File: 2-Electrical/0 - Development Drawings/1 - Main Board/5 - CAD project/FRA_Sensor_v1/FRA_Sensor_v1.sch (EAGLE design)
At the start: 237 parts, among them IC1 CP2101, IC2 LMV611, IC3 TS520533, IC4 ADS1115BQDGSRQ1, IC5 ADS1115BQDGSRQ1, IC7 LMP91000SD_NOPB, IC8 PCA9555PW, IC9 LDK320ADU50R, J2 ETH_CONN, J5 WM9734TR-ND, J8 1140084168, Q1 Si2300DS, Q10 FDN306P, Q11 FDN306P, Q12 FDN306P, Q13 FDN306P, Q14 FDN306P, Q15 FDN306P, Q16 FDN306P, Q17 FDN306P, Q2 FDN306P, Q3 Si2300DS, Q5 FDN306P, Q6 FDN306P, Q7 100A/100V/6.8mΩ, Q8 FDN306P, Q9 FDN306P, T1 BC847, T2 BC847, T3 BC847, U1 PCA9509DP, U2 ESP-WROOM-32, X1 TB001-500-02BE, Y3 32.768kHz

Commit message: sch update layout update
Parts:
- removed C20, C22: 10u, resistor:C-EUC0603K
- removed C32, C33, C34: 100n, resistor:C-EUC0603K
- removed C35, C36: 1u, resistor:C-EUC0603K
- removed D3: BAS17, nxp_60:BAS17
- removed IC3: TS520533, v-reg:TS520533
- removed IC7: LMP91000SD_NOPB, SamacSys_Parts:LMP91000SD_NOPB
- removed Q1: Si2300DS, adafruit:MOSFET-NREFLOW
- removed Q16, Q17: FDN306P, microbuilder:MOSFET-PWIDE
- removed R33, R66, R79, R80: 10k, resistor:R-EU_R0603
- removed R34, R35, R36: 47k, resistor:R-EU_R0603
- removed R37: 27k, resistor:R-EU_R0603
- removed R38: 0, resistor:R-EU_R0603
- removed R39: 12k, resistor:R-EU_R0603
- removed R56: 5.1k, resistor:R-EU_R0603
- removed R57: 0R, resistor:R-EU_R0603
- removed R58, R60, R61, R62: (DNI), resistor:R-EU_R0603
- removed R59: 1M, resistor:R-EU_R0603
- removed S$1: CITIPEL_4P50, FRA_eagle_lib:CITIPEL_4P50
- removed S$2: FIGARO_2611, FRA_eagle_lib:FIGARO_2611
- removed T3: BC847, nxp_60:BC847
- removed T4: (no value), transistor-neu-to92:-NPN-SOT223
- removed TP18: TPTP10R, testpad:TPTP10R
- removed U$17, U$18: CONN_03X2_WE_61200621621, FRA_eagle_lib:CONN_03X2_WE_61200621621
- added R14: 0(DNI), resistor:R-EU_R0603
- added R15, R18: 10k, resistor:R-EU_R0603
- added SENSOR_D3: + G SCL SDA, pinhead:PINHD-1X4
- added TP21: TPTP10R, testpad:TPTP10R
- C18: value 1n -> 100n
- C19: value 10u -> 100n
- C37, C41: value 1u -> 10u
- C4: value 1u -> 100n
- IC2: value LMV611 -> ADS1115BQDGSRQ1; device linear:OPA333DCK -> SamacSys_Parts:ADS1115BQDGSRQ1
- R42: value 2k(NC) -> 10k
- R81, R82: value 10k -> 2k2
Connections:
- removed net 3V3_TGS2611: C36.1, IC3.VOUT, R61.2
- removed net AA1: R66.1
- removed net ADC3_3: U$17.2
- removed net ADC3_4: U$18.2
- removed net ADC_TGS2611: C33.1, R57.2, R58.2
- removed net ENB_PWR_IF11: Q16.G, R79.2
- removed net ENB_PWR_IF12: Q17.G, R80.2
- removed net EN_IF11: Q16.D, R79.1, U$17.4
- removed net EN_IF12: Q17.D, R80.1, U$18.4
- removed net N$12 (its old number): C22.1, C4.1, R66.2
- removed net N$13 (its old number): C22.2
- removed net N$14: C4.2
- removed net N$16: IC2.V+
- removed net N$17: R38.1
- removed net N$18: R34.2
- removed net N$26: R39.1, T3.B
- removed net N$27: C18.1
- removed net N$28: IC2.+IN, R34.1, R35.2
- removed net N$32: IC2.-IN, R36.2, R37.1
- removed net N$34: C19.1, R37.2
- removed net N$35: IC2.OUT, R36.1
- removed net N$36: C18.2, C19.2, R33.2, R39.2
- removed net N$46: IC8.I/O1.4, TP18.TP
- removed net N$53: Q1.D, S$2.1_RH
- removed net N$56: C34.1, IC3.CB
- removed net PWM: R33.1
- removed net RS_NEG: R56.1, R57.1, S$2.2_RS_N
- removed net RS_POS: C32.1, R60.2, R61.1, R62.1, S$2.3_RS_P
- removed net TGS2611_HEAT_EN: Q1.G, R59.1
- removed net VREF_TGS6211: R62.2
- new net 3AIN0: C18.1, IC2.AIN1, R15.1
- new net 3AIN1: C19.1, IC2.AIN2, R18.1
- new net N$7: IC2.ALERT/RDY, TP21.TP
- net +5V/1: now also C4.1, C42.1, IC2.VDD, R67.1, R70.1, R71.1, R72.1, R73.1, R74.1, R75.1, R76.1, R77.1, R78.1; no longer Q16.S, Q17.S
- net 1AIN0: now also IC5.AIN2; no longer IC5.AIN0
- net 1AIN1: now also IC5.AIN3; no longer IC5.AIN1
- net 1AIN2: now also IC5.AIN1; no longer IC5.AIN3
- net 1AIN3: now also IC5.AIN0; no longer IC5.AIN2
- net 2AIN0: now also IC4.AIN2; no longer IC4.AIN0
- net 2AIN1: now also IC4.AIN3; no longer IC4.AIN1
- net 2AIN2: now also IC4.AIN1; no longer IC4.AIN3
- net 2AIN3: now also IC4.AIN0; no longer IC4.AIN2
- net 5V: no longer C35.1, C42.1, IC3.CE, IC3.VIN, R60.1, S$2.4_RH
- net 5V_CALM: no longer U$17.3, U$18.3
- net ADC3_1: now also R15.2
- net ADC3_2: now also R18.2
- net AGND: now also C18.2, C19.2, C4.2, IC2.GND; no longer U$17.1, U$18.1
- net BTN1: now also R14.2
- net ENB_PWR_IF1: now also IC8.I/O0.6; no longer IC8.I/O0.0
- net ENB_PWR_IF10: now also IC8.I/O0.0
- net ENB_PWR_IF2: now also IC8.I/O0.7; no longer IC8.I/O0.1
- net ENB_PWR_IF7: now also IC8.I/O1.7; no longer IC8.I/O0.6
- net ENB_PWR_IF8: now also IC8.I/O1.6; no longer IC8.I/O0.7
- net ENB_PWR_IF9: now also IC8.I/O0.1
- net EN_IF1: no longer R67.1
- net EN_IF10: no longer R78.1
- net EN_IF2: no longer R70.1
- net EN_IF3: no longer R71.1
- net EN_IF4: no longer R72.1
- net EN_IF5: no longer R73.1
- net EN_IF6: no longer R74.1
- net EN_IF7: no longer R75.1
- net EN_IF8: no longer R76.1
- net EN_IF9: no longer R77.1
- net GND: no longer C32.2, C33.2, C34.2, C35.2, C36.2, IC3.GND, Q1.S, R38.2, R56.2, R58.1, R59.2, T3.E
- net NRST: now also R14.1
- net SCL_5V: now also IC2.ADDR, IC2.SCL; no longer U$17.6, U$18.6
- net SDA_5V: now also IC2.SDA; no longer U$17.5, U$18.5
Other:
- note added: "GY-21 Si7021 - T a RH addr:0x40"
- note added: "Molex 105133-0001"
- note added: "VEML7700 - Lux addr:0X10"
- note added: "pull-downs on sensor boards"
- note removed: "15.9kHz cutoff"
- note removed: "3.3V LDO"
- note removed: "Buzzer audio"
- note removed: "DNI"
- note removed: "For capacitance multiplier 621-FZT651QTC - 3A Ic 621-FZT851QTA - 6A Ic"
- note removed: "GY-21 Si7021 - T a RH addr:0x40 VEML7700 - Lux addr:0X10"
- note removed: "TODO LDO to 5V low noise supply"
- note removed: "alt. part LP5907"

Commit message: layout done,
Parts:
- renumbered SENSOR_D1 to S_D1, SENSOR_D2 to S_D2
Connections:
- removed net BTN2: U2.IO35
- new net N$14: IC2.AIN0, SENSOR_D3.3
- new net N$16: IC2.AIN3, SENSOR_D3.2
- net +5V/1: now also SENSOR_D3.4
- net AGND: now also SENSOR_D3.1
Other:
- moved on the sheet: SENSOR_D3

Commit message: updates
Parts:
- removed FID3: FIDUCIAL"", microbuilder:FIDUCIAL""
- added C20: 10u, resistor:C-EUC0603K
- added C22: 100n, resistor:C-EUC0603K
- added IC3: P82B715DR, SamacSys_Parts:P82B715DR
- added R33, R34: 330, resistor:R-EU_R0603
- R21: value 1M -> 100k
- R3: value 470 -> 100
- renumbered SENSOR_D3 to J9
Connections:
- new net SCL_BUFF: IC3.LY, R34.2, U$10.6, U$11.6, U$12.6, U$13.6, U$14.6, U$15.6, U$16.6, U$3.6, U$8.6, U$9.6
- new net SDA_BUFF: IC3.LX, R33.2, U$10.5, U$11.5, U$12.5, U$13.5, U$14.5, U$15.5, U$16.5, U$3.5, U$8.5, U$9.5
- net +5V/1: now also C20.1, C22.1, IC3.VCC, R33.1, R34.1
- net AGND: now also C20.2, C22.2, IC3.GND
- net SCL_5V: now also IC3.SY; no longer U$10.6, U$11.6, U$12.6, U$13.6, U$14.6, U$15.6, U$16.6, U$3.6, U$8.6, U$9.6
- net SDA_5V: now also IC3.SX; no longer U$10.5, U$11.5, U$12.5, U$13.5, U$14.5, U$15.5, U$16.5, U$3.5, U$8.5, U$9.5
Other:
- note added: "A3.0,A3.3"
- note added: "ADC1"
- note added: "ADC2"
- note added: "ADC3"
- note added: "I2C repeater"
- note added: "Pullup min 270R (due to sink current)"
- moved on the sheet: C18, C19, C21, C46, C47, C48, C49, C50, C51, C52, R15, R18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

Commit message: updates
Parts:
- removed J1: (no value), con-jack:JACK-PLUG1
- added J3: PJ-031C, SamacSys_Parts:PJ-031C
- C1, C12, C13, C15, C18, C19, C21, C22, C23, C27, C28, C3, C31, C38, C4, C40, C42, C43, C44, C45, C46, C47, C48, C49, C5, C50, C51, C52, C9: PARTNO (none) -> CC0603KRX7R8BB104
- C11, C2, C20, C24, C25, C26, C39, C41, C8: PARTNO (none) -> GRM188R61A106KE69J
- C14, C37, C6: PARTNO (none) -> GRM188R61E106KA73J
- C16: PARTNO (none) -> C0603C102M5RACTU
- C29, C30: PARTNO (none) -> C0402C220J5GAC7411
- C7: PARTNO (none) -> EMZR250ARA221MF80G
- D1, D2, D4, D6: PARTNO (none) -> PESD1CAN-UX
- D8: value (none) -> LTL2R3KGD-EM; PARTNO (none) -> LTL2R3KGD-EM
- FAN_5V: PARTNO (none) -> 640456-2
- FB1, FB2, FB3, FB4, FB5, FB6, FB7, FB8, FB9: PARTNO (none) -> BLM18PG121SN1D
- IC1: PARTNO (none) -> CP2101-GM
- IC2, IC4, IC5: value ADS1115BQDGSRQ1 -> ADS1115IDGSR; PARTNO (none) -> ADS1115IDGSR
- IC3: PARTNO (none) -> P82B715DR
- IC9: PARTNO (none) -> LDK320ADU50R
- J2: PARTNO (none) -> CES-106-01-T-D
- J4: PARTNO (none) -> GSD090012SEU
- J5: PARTNO (none) -> Molex 105133-0001
- J8: PARTNO (none) -> 1140084168
- J9: PARTNO (none) -> 61300411121
- JTAG1: PARTNO (none) -> M50-3600542R
- L2, L3: PARTNO (none) -> SRN6045TA-1R5Y
- Q10, Q11, Q12, Q13, Q14, Q15, Q2, Q5, Q6, Q8, Q9: PARTNO (none) -> FDN306P
- Q3: PARTNO (none) -> SI2300DS-T1-GE3
- Q7: value 100A/100V/6.8mΩ -> DNI
- R1, R2: PARTNO (none) -> RC0603FR-0712KL
- R10, R12, R13, R19, R24, R3: PARTNO (none) -> CRCW0603100RFKEAC
- R11, R16, R32, R4, R43, R46, R47, R5, R6, R65, R7, R8: PARTNO (none) -> CRCW06030000Z0EAC
- R14: value 0(DNI) -> DNI; PARTNO (none) -> CRCW06030000Z0EAC
- R15, R18, R22, R42, R49, R67, R70, R71, R72, R73, R74, R75, R76, R77, R78, R83, R84, R85, R86, R87, R88, R89, R90: PARTNO (none) -> CRCW060310K0JNEAC
- R17, R20, R31, R48, R55, R63: PARTNO (none) -> CRCW060347R0FKEAC
- R21, R53, R54, R9: PARTNO (none) -> CRCW0603100KFKEAC
- R23: value 5k(DNI) -> DNI; PARTNO (none) -> CRCW06030000Z0EAC
- R25, R64, R68: value 10K -> 10k; PARTNO (none) -> CRCW060310K0JNEAC
- R26, R27: PARTNO (none) -> CRCW060310R0FKEAC
- R28, R50: value 10k -> 10k/1%; PARTNO (none) -> RN73R1JTTD1002D25
- R30: PARTNO (none) -> ERJ-PB3D4532V
- R33, R34: PARTNO (none) -> CRCW0603330RFKEAC
- R40: value 10k(NC) -> DNI; PARTNO (none) -> CRCW06030000Z0EAC
- R44: value (NC) -> DNI; PARTNO (none) -> CRCW06030000Z0EAC
- R52: PARTNO (none) -> ERJ-PB3D7322V
- R81, R82: PARTNO (none) -> CRGCQ0603F2K2
- S1: PARTNO (none) -> B3F-3120
- S_D1, S_D2: value + G SCL SDA -> 4pin; PARTNO (none) -> 61300411121
- T1, T2: PARTNO (none) -> BC847A-TP
- U$1, U$4: value TPS5632149DDCR -> TPS563249DDCR; PARTNO (none) -> TPS563249DDCR
- U$10, U$11, U$12, U$13, U$14, U$15, U$16, U$3, U$8, U$9: PARTNO (none) -> Wurth 61200621621
- U$2: PARTNO (none) -> HTMS-103-03-T-D-SM
- U1: PARTNO (none) -> PCA9509DP,118
- U2: PARTNO (none) -> ESP32-WROOM-32
- X1: PARTNO (none) -> TB001-500-02BE
- Y3: PARTNO (none) -> FC-135 32.7680KA-A3
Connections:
- net GNDIN: now also J3.2, J3.3; no longer J1.1, J1.2
- net VIN_IN: now also J3.1; no longer J1.3
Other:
- note added: "5k"

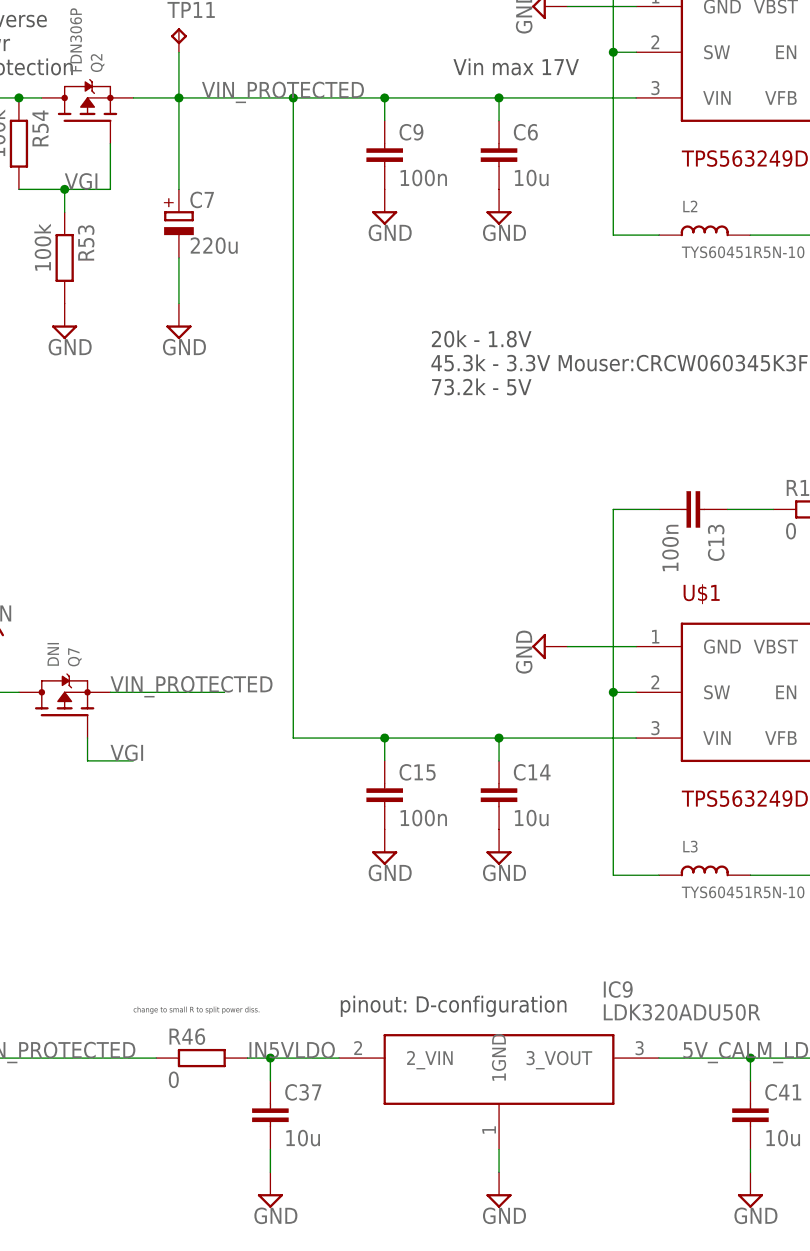
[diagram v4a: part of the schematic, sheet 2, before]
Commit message: SD and ethernet merged
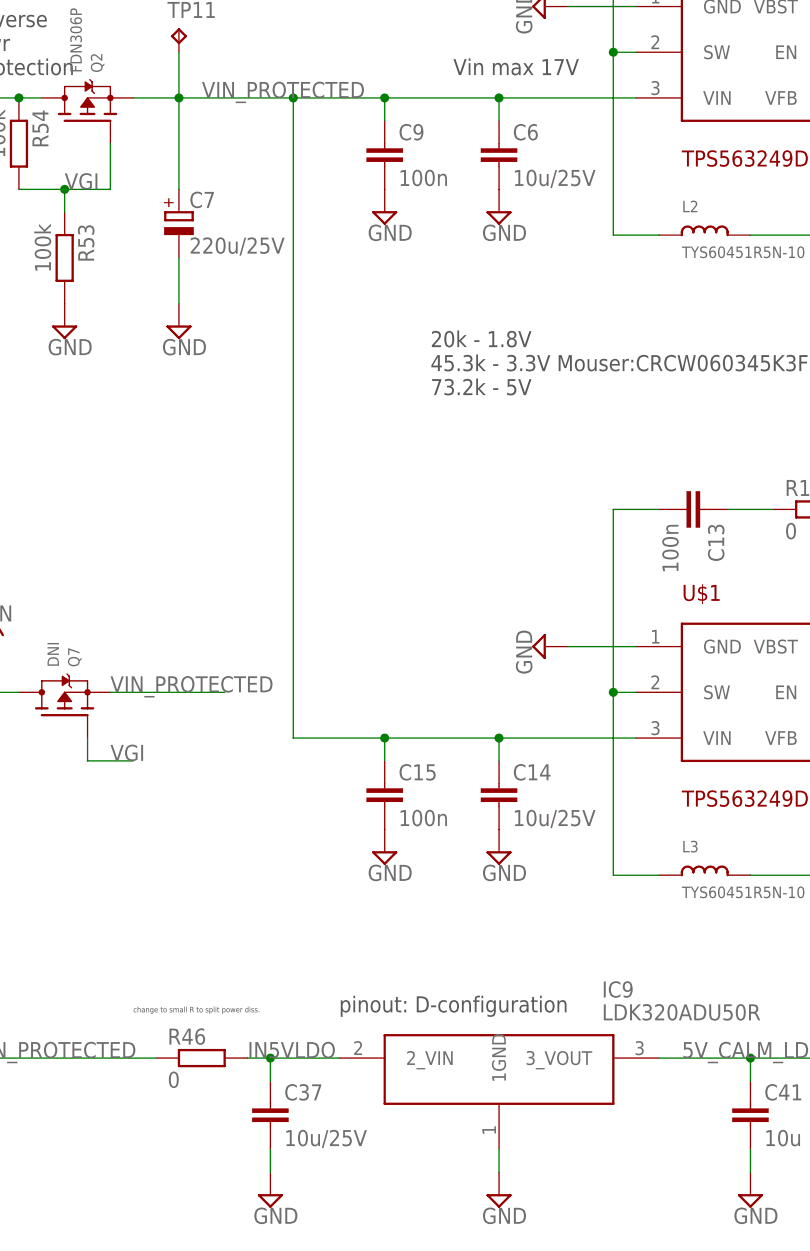
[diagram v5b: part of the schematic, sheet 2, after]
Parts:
- C14, C37, C6: value 10u -> 10u/25V
- C7: value 220u -> 220u/25V
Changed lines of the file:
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@@
 <attribute name="PARTNO" value="CRCW06030000Z0EAC"/>
 </part>
-<part name="C6" library="resistor" deviceset="C-EU" device="C0603K" value="10u">
+<part name="C6" library="resistor" deviceset="C-EU" device="C0603K" value="10u/25V">
 <attribute name="PARTNO" value="GRM188R61E106KA73J"/>
 </part>
@@
 <attribute name="PARTNO" value="CRCW06030000Z0EAC"/>
 </part>
-<part name="C14" library="resistor" deviceset="C-EU" device="C0603K" value="10u">
+<part name="C14" library="resistor" deviceset="C-EU" device="C0603K" value="10u/25V">
 <attribute name="PARTNO" value="GRM188R61E106KA73J"/>
 </part>
@@
 <attribute name="PARTNO" value="TB001-500-02BE"/>
 </part>
-<part name="C7" library="resistor" deviceset="CPOL-EU" device="153CLV-0605" value="220u">
+<part name="C7" library="resistor" deviceset="CPOL-EU" device="153CLV-0605" value="220u/25V">
 <attribute name="PARTNO" value="EMZR250ARA221MF80G"/>
 </part>
@@
 <part name="FID2" library="microbuilder" deviceset="FIDUCIAL" device="&quot;&quot;"/>
 <part name="FID4" library="microbuilder" deviceset="FIDUCIAL" device="&quot;&quot;"/>
-<part name="C37" library="resistor" deviceset="C-EU" device="C0603K" value="10u">
+<part name="C37" library="resistor" deviceset="C-EU" device="C0603K" value="10u/25V">
 <attribute name="PARTNO" value="GRM188R61E106KA73J"/>
 </part>

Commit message: Update FRA_Sensor_v1.sch
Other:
- note added: "Multicomp MC34459 Mouser GSD090012SEU - not correct"
- note removed: "Multicomp MC34459 Mouser GSD090012SEU"
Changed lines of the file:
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@@
 <text x="182.88" y="48.26" size="1.778" layer="97">female</text>
 <text x="12.7" y="50.8" size="1.778" layer="97">RTC DNI</text>
-<text x="223.52" y="86.36" size="1.778" layer="97">Multicomp MC34459
-Mouser GSD090012SEU</text>
+<text x="220.98" y="81.28" size="1.778" layer="97">Multicomp MC34459
+Mouser GSD090012SEU - not correct</text>
 <text x="106.68" y="86.36" size="1.778" layer="97">5k</text>
 </plain>

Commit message: boad update v2
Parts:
- removed D8: LTL2R3KGD-EM, SparkFun-LED:LED5MM
- removed R46: 0, resistor:R-EU_R0603
- added C32: 100n, resistor:C-EUC0603K
- added FB10: (no value), microbuilder:FERRITE
- added LED_HDR: 2pin, pinhead:PINHD-1X2
- added R35: 0, resistor:R-EU_R0603
- added R36, R37: DNI, resistor:R-EU_R0603
- C10: value DNI -> 10u/25V
- C16: value 1n -> 10u
- C17: value DNI -> 10u
- IC8: PARTNO (none) -> PCA9555PW,118
- J3: value PJ-031C -> PJ-059A; device SamacSys_Parts:PJ-031C -> FRA_eagle_lib:PJ-059A
- L2, L3: value TYS60451R5N-10 1.5uH -> SRP5030CA-1R5M; device FRA_eagle_lib:INDUCTOR6X6MM -> FRA_eagle_lib:SRP5030CA-1R5M
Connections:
- new net N$17: IC8.A2, R35.1, R36.2
- net +5V/1: now also C32.1, R36.1
- net 5V: now also R37.2
- net AGND: now also C32.2, R35.2; no longer IC8.A2
- net ETH_5V: now also R37.1
- net GND: no longer IC1.GND@M
- net IN5VLDO: now also FB10.P$2; no longer R46.2
- net LED: now also LED_HDR.1; no longer D8.C
- net N$6: now also LED_HDR.2; no longer D8.A
- net VIN_PROTECTED: now also FB10.P$1; no longer R46.1
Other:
- moved on the sheet: J3
